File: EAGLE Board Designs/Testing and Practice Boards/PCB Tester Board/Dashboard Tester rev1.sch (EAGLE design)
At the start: 32 parts, among them J1 CONNECTOR-CAN_NF_T_V_BLACK, J2 CONNECTOR-6_NF_T_V_BLACK, J3 CONNECTOR-8_NF_T_V_BLACK, Q1 TRANSISTOR_N_MOS_PMV15ENEA, Q10 TRANSISTOR_N_MOS_PMV15ENEA, Q11 TRANSISTOR_P_MOS_SOT23_SI2369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, Q2 TRANSISTOR_N_MOS_PMV15ENEA, Q3 TRANSISTOR_N_MOS_PMV15ENEA, Q4 TRANSISTOR_N_MOS_PMV15ENEA, Q5 TRANSISTOR_N_MOS_PMV15ENEA, Q6 TRANSISTOR_N_MOS_PMV15ENEA, Q7 TRANSISTOR_P_MOS_SOT23_SI2369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, Q8 TRANSISTOR_N_MOS_PMV15ENEA, Q9 TRANSISTOR_P_MOS_SOT23_SI2369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, U1 TEENSY_3.5, U2 CAN_TRANSCIEVER_TCAN1051HQV-Q1, U3 VOLTAGE_REGULATOR_OKI-78SR_5V

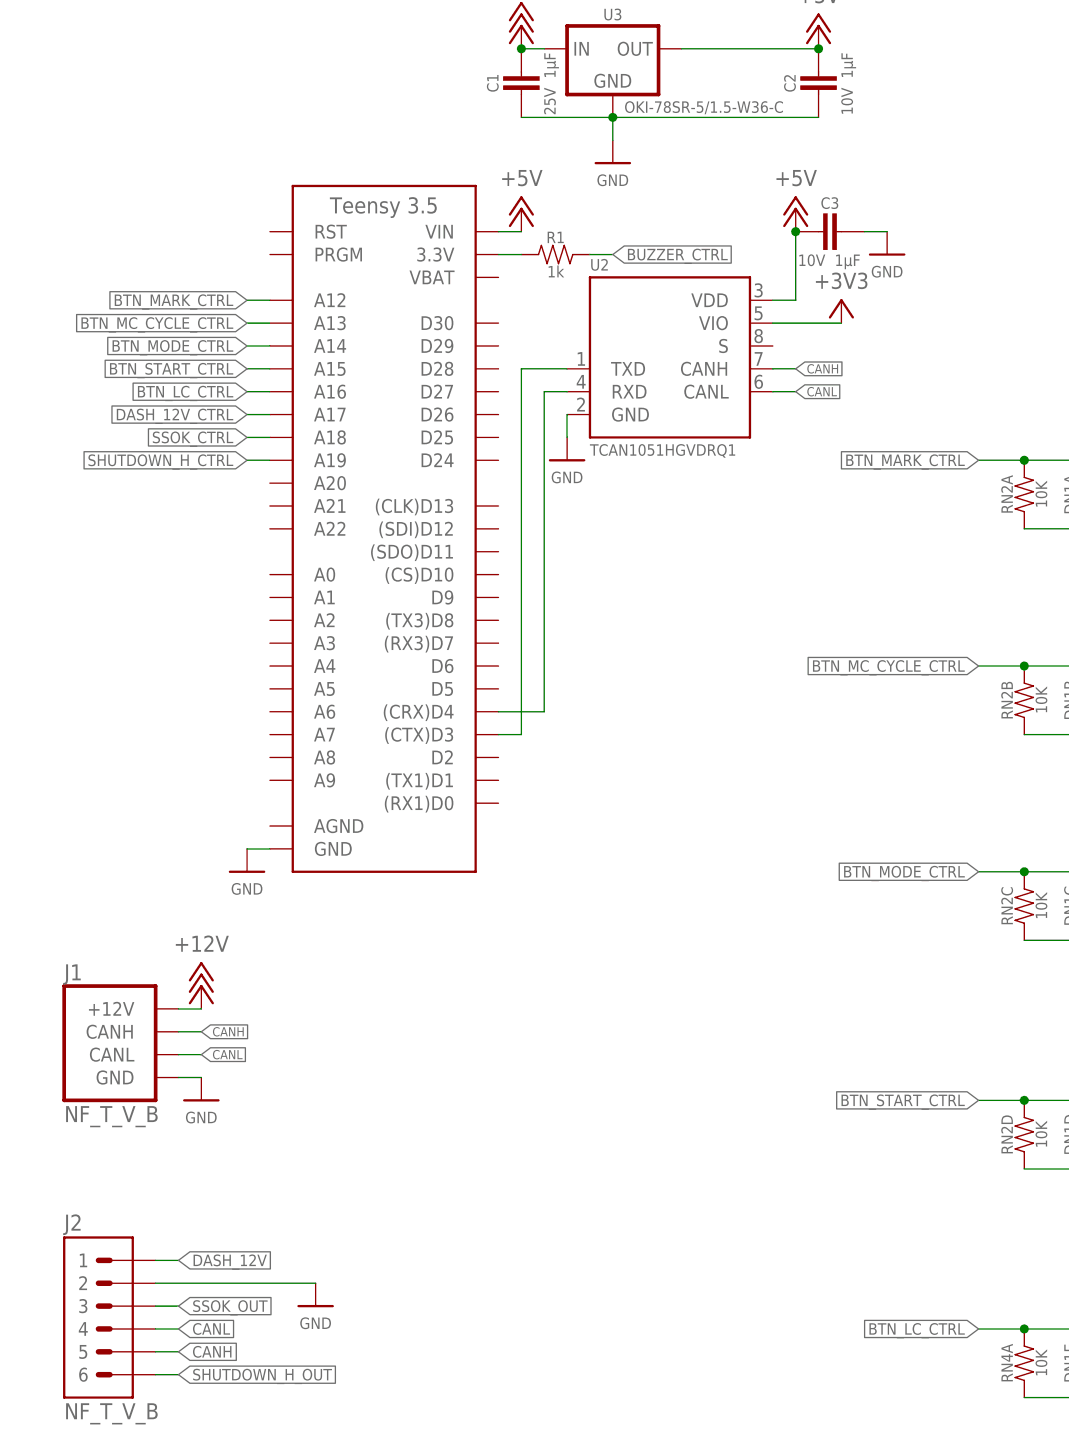
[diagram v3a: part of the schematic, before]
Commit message: Rearranged control-teensy connections
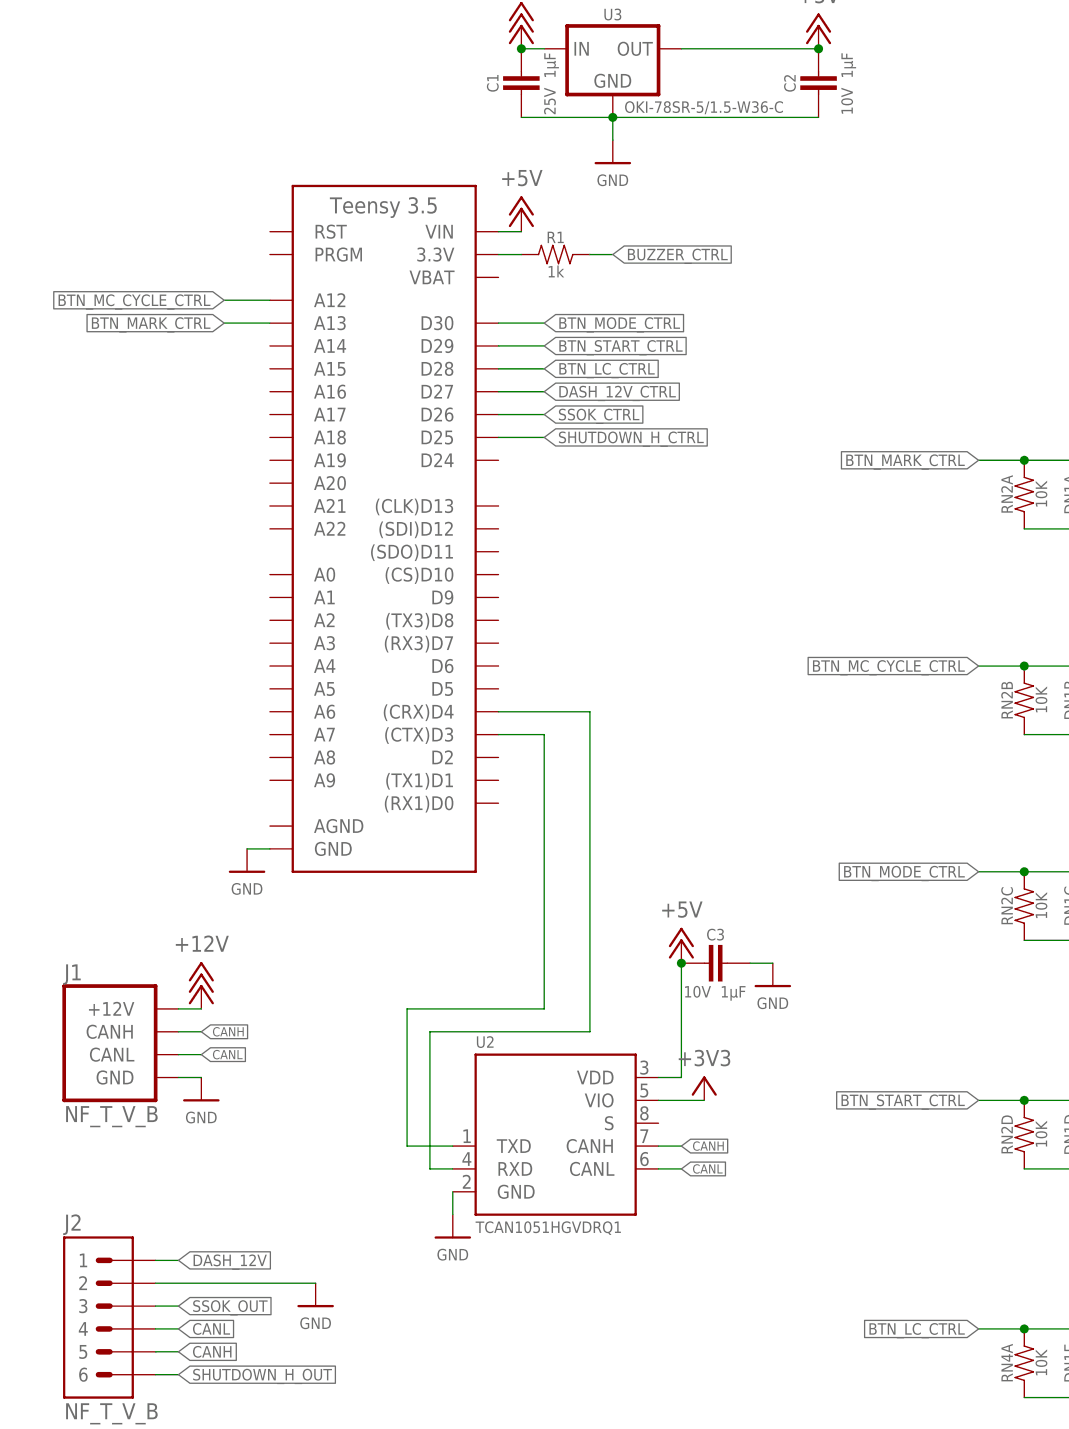
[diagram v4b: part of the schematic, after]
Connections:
- removed net N$5: U1.A17
- net BTN_LC_CTRL: now also U1.D28; no longer U1.A16
- net BTN_MARK_CTRL: now also U1.A13; no longer U1.A12
- net BTN_MC_CYCLE_CTRL: now also U1.A12; no longer U1.A13
- net BTN_MODE_CTRL: now also U1.D30; no longer U1.A14
- net BTN_START_CTRL: now also U1.D29; no longer U1.A15
- net DASH_12V_CTRL: now also U1.D27
- net SHUTDOWN_H_CTRL: now also U1.D25; no longer U1.A19
- net SSOK_CTRL: now also U1.D26; no longer U1.A18
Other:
- moved on the sheet: C3, U2

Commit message: Continuing trace work
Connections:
- removed net BUZZER_CTRL: J3.4
- net BTN_LAUNCH_CONTROL: now also J3.4; no longer J3.7
- net BTN_MARK: now also J3.8; no longer J3.2
- net BTN_MC_CYCLE: now also J3.7; no longer J3.3
- net BTN_MODE: now also J3.6; no longer J3.5
- net BTN_START: now also J3.5; no longer J3.6
- net DASH_12V: now also J3.1
- net SHUTDOWN_H_OUT: now also J3.3
- net SSOK_OUT: now also J3.2
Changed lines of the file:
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@@
 <label x="25.4" y="55.88" size="1.27" layer="95" xref="yes"/>
+</segment>
+<segment>
+<wire x1="22.86" y1="30.48" x2="27.94" y2="30.48" width="0.1524" layer="91"/>
+<label x="27.94" y="30.48" size="1.27" layer="95" xref="yes"/>
+<pinref part="J3" gate="G$1" pin="2"/>
 </segment>
 </net>
@@
 <label x="25.4" y="60.96" size="1.27" layer="95" xref="yes"/>
 </segment>
+<segment>
+<wire x1="22.86" y1="33.02" x2="27.94" y2="33.02" width="0.1524" layer="91"/>
+<label x="27.94" y="33.02" size="1.27" layer="95" xref="yes"/>
+<pinref part="J3" gate="G$1" pin="1"/>
+</segment>
 </net>
 <net name="SHUTDOWN_H_OUT" class="0">
@@
 <wire x1="22.86" y1="48.26" x2="25.4" y2="48.26" width="0.1524" layer="91"/>
 <label x="25.4" y="48.26" size="1.27" layer="95" xref="yes"/>
+</segment>
+<segment>
+<wire x1="22.86" y1="27.94" x2="27.94" y2="27.94" width="0.1524" layer="91"/>
+<label x="27.94" y="27.94" size="1.27" layer="95" xref="yes"/>
+<pinref part="J3" gate="G$1" pin="3"/>
 </segment>
 </net>
@@
 <net name="BTN_MARK" class="0">
 <segment>
-<pinref part="J3" gate="G$1" pin="2"/>
-<wire x1="22.86" y1="30.48" x2="25.4" y2="30.48" width="0.1524" layer="91"/>
-<label x="25.4" y="30.48" size="1.27" layer="95" xref="yes"/>
-</segment>
-<segment>
 <pinref part="Q1" gate="G$1" pin="D"/>
 <wire x1="149.86" y1="154.94" x2="154.94" y2="154.94" width="0.1524" layer="91"/>
 <label x="154.94" y="154.94" size="1.27" layer="95" xref="yes"/>
 </segment>
+<segment>
+<wire x1="22.86" y1="15.24" x2="27.94" y2="15.24" width="0.1524" layer="91"/>
+<label x="27.94" y="15.24" size="1.27" layer="95" xref="yes"/>
+<pinref part="J3" gate="G$1" pin="8"/>
+</segment>
 </net>
 <net name="BTN_MC_CYCLE" class="0">
-<segment>
-<pinref part="J3" gate="G$1" pin="3"/>
-<wire x1="22.86" y1="27.94" x2="25.4" y2="27.94" width="0.1524" layer="91"/>
-<label x="25.4" y="27.94" size="1.27" layer="95" xref="yes"/>
-</segment>
 <segment>
 <pinref part="Q2" gate="G$1" pin="D"/>
@@
 <label x="154.94" y="132.08" size="1.27" layer="95" xref="yes"/>
 </segment>
-</net>
-<net name="BUZZER_CTRL" class="0">
 <segment>
-<pinref part="J3" gate="G$1" pin="4"/>
-<wire x1="22.86" y1="25.4" x2="25.4" y2="25.4" width="0.1524" layer="91"/>
-<label x="25.4" y="25.4" size="1.27" layer="95" xref="yes"/>
-<label x="73.66" y="172.72" size="1.27" layer="95" xref="yes"/>
+<wire x1="22.86" y1="17.78" x2="27.94" y2="17.78" width="0.1524" layer="91"/>
+<label x="27.94" y="17.78" size="1.27" layer="95" xref="yes"/>
+<pinref part="J3" gate="G$1" pin="7"/>
 </segment>
 </net>
 <net name="BTN_MODE" class="0">
-<segment>
-<pinref part="J3" gate="G$1" pin="5"/>
-<wire x1="22.86" y1="22.86" x2="25.4" y2="22.86" width="0.1524" layer="91"/>
-<label x="25.4" y="22.86" size="1.27" layer="95" xref="yes"/>
-</segment>
 <segment>
 <pinref part="Q3" gate="G$1" pin="D"/>
@@
 <label x="154.94" y="109.22" size="1.27" layer="95" xref="yes"/>
 </segment>
+<segment>
+<wire x1="22.86" y1="20.32" x2="27.94" y2="20.32" width="0.1524" layer="91"/>
+<label x="27.94" y="20.32" size="1.27" layer="95" xref="yes"/>
+<pinref part="J3" gate="G$1" pin="6"/>
+</segment>
 </net>
 <net name="BTN_START" class="0">
-<segment>
-<pinref part="J3" gate="G$1" pin="6"/>
-<wire x1="22.86" y1="20.32" x2="25.4" y2="20.32" width="0.1524" layer="91"/>
-<label x="25.4" y="20.32" size="1.27" layer="95" xref="yes"/>
-</segment>
 <segment>
 <pinref part="Q4" gate="G$1" pin="D"/>
@@
 <label x="154.94" y="83.82" size="1.27" layer="95" xref="yes"/>
 </segment>
+<segment>
+<wire x1="22.86" y1="22.86" x2="27.94" y2="22.86" width="0.1524" layer="91"/>
+<label x="27.94" y="22.86" size="1.27" layer="95" xref="yes"/>
+<pinref part="J3" gate="G$1" pin="5"/>
+</segment>
 </net>
 <net name="BTN_LAUNCH_CONTROL" class="0">
-<segment>
-<pinref part="J3" gate="G$1" pin="7"/>
-<wire x1="22.86" y1="17.78" x2="25.4" y2="17.78" width="0.1524" layer="91"/>
-<label x="25.4" y="17.78" size="1.27" layer="95" xref="yes"/>
-</segment>
 <segment>
 <pinref part="Q5" gate="G$1" pin="D"/>
@@
 <label x="154.94" y="58.42" size="1.27" layer="95" xref="yes"/>
 </segment>
+<segment>
+<wire x1="22.86" y1="25.4" x2="27.94" y2="25.4" width="0.1524" layer="91"/>
+<label x="27.94" y="25.4" size="1.27" layer="95" xref="yes"/>
+<pinref part="J3" gate="G$1" pin="4"/>
+</segment>
 </net>

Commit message: Finished tracing
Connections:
- net BTN_LAUNCH_CONTROL: now also J3.1; no longer J3.4
- net DASH_12V: now also J3.4; no longer J3.1
- net SHUTDOWN_H_OUT: no longer J3.3
- net SSOK_OUT: no longer J3.2
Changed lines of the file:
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@@
 <label x="25.4" y="55.88" size="1.27" layer="95" xref="yes"/>
-</segment>
-<segment>
-<wire x1="22.86" y1="30.48" x2="27.94" y2="30.48" width="0.1524" layer="91"/>
-<label x="27.94" y="30.48" size="1.27" layer="95" xref="yes"/>
-<pinref part="J3" gate="G$1" pin="2"/>
 </segment>
 </net>
@@
 </segment>
 <segment>
-<wire x1="22.86" y1="33.02" x2="27.94" y2="33.02" width="0.1524" layer="91"/>
-<label x="27.94" y="33.02" size="1.27" layer="95" xref="yes"/>
-<pinref part="J3" gate="G$1" pin="1"/>
+<wire x1="22.86" y1="25.4" x2="27.94" y2="25.4" width="0.1524" layer="91"/>
+<label x="27.94" y="25.4" size="1.27" layer="95" xref="yes"/>
+<pinref part="J3" gate="G$1" pin="4"/>
 </segment>
 </net>
@@
 <wire x1="22.86" y1="48.26" x2="25.4" y2="48.26" width="0.1524" layer="91"/>
 <label x="25.4" y="48.26" size="1.27" layer="95" xref="yes"/>
-</segment>
-<segment>
-<wire x1="22.86" y1="27.94" x2="27.94" y2="27.94" width="0.1524" layer="91"/>
-<label x="27.94" y="27.94" size="1.27" layer="95" xref="yes"/>
-<pinref part="J3" gate="G$1" pin="3"/>
 </segment>
 </net>
@@
 </segment>
 <segment>
-<wire x1="22.86" y1="25.4" x2="27.94" y2="25.4" width="0.1524" layer="91"/>
-<label x="27.94" y="25.4" size="1.27" layer="95" xref="yes"/>
-<pinref part="J3" gate="G$1" pin="4"/>
+<wire x1="22.86" y1="33.02" x2="27.94" y2="33.02" width="0.1524" layer="91"/>
+<label x="27.94" y="33.02" size="1.27" layer="95" xref="yes"/>
+<pinref part="J3" gate="G$1" pin="1"/>
 </segment>
 </net>

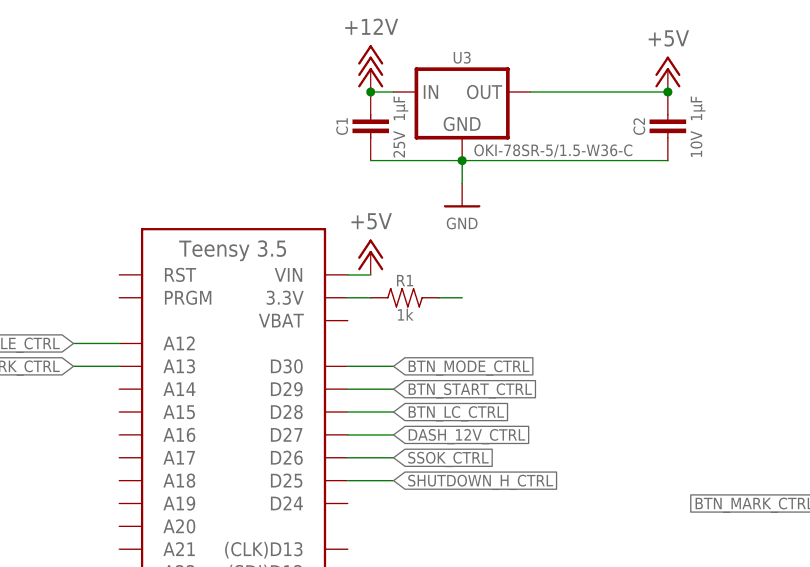
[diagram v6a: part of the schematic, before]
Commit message: Fixed 3v3 connection
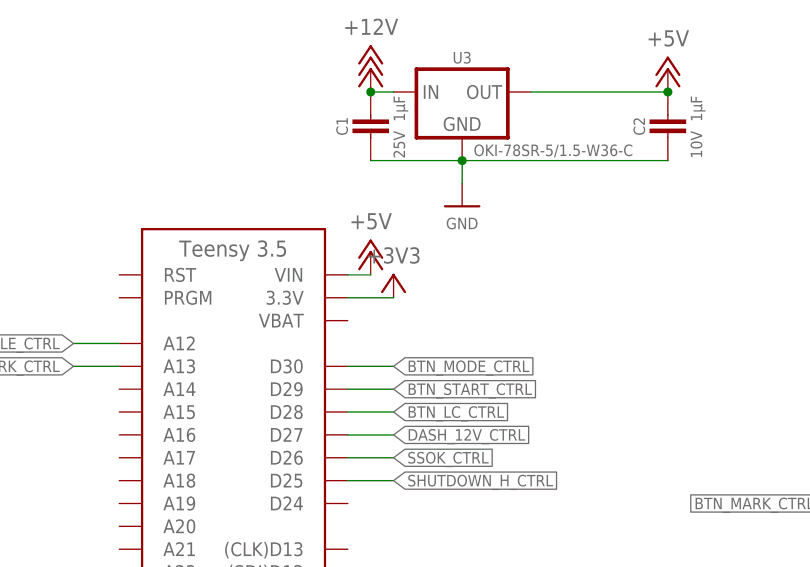
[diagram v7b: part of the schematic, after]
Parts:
- removed R1: 1k, HyTechDevices:RESISTOR0603
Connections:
- removed net N$7: R1.1, U1.3.3V
- removed net N$9: R1.2
- net +3V3: now also U1.3.3V
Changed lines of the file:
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@@
 <part name="C3" library="HyTechDevices" deviceset="CAPACITOR_?_*" device="0603" technology="10V_1UF"/>
 <part name="GND14" library="HyTechSupplies" deviceset="GND" device=""/>
-<part name="R1" library="HyTechDevices" deviceset="RESISTOR" device="0603" value="1k"/>
+<part name="+3V2" library="HyTechSupplies" deviceset="+3V3" device=""/>
 </parts>
 <sheets>
@@
 <attribute name="VALUE" x="91.44" y="90.17" size="1.27" layer="96" align="top-center"/>
 </instance>
-<instance part="R1" gate="G$1" x="68.58" y="172.72" smashed="yes">
-<attribute name="NAME" x="67.31" y="173.99" size="1.27" layer="95" align="bottom-center"/>
-<attribute name="VALUE" x="67.31" y="171.45" size="1.27" layer="96" align="top-center"/>
+<instance part="+3V2" gate="G$1" x="66.04" y="175.26" smashed="yes">
+<attribute name="VALUE" x="66.04" y="176.53" size="1.778" layer="96" align="bottom-center"/>
 </instance>
 </instances>
@@
 <wire x1="78.74" y1="78.74" x2="83.82" y2="78.74" width="0.1524" layer="91"/>
 </segment>
+<segment>
+<pinref part="+3V2" gate="G$1" pin="+3V3"/>
+<wire x1="60.96" y1="172.72" x2="66.04" y2="172.72" width="0.1524" layer="91"/>
+<pinref part="U1" gate="G$1" pin="3.3V"/>
+</segment>
 </net>
 <net name="CANH" class="0">
@@
 </segment>
 </net>
-<net name="N$7" class="0">
-<segment>
-<pinref part="U1" gate="G$1" pin="3.3V"/>
-<pinref part="R1" gate="G$1" pin="1"/>
-<wire x1="60.96" y1="172.72" x2="63.5" y2="172.72" width="0.1524" layer="91"/>
-</segment>
-</net>
-<net name="N$9" class="0">
-<segment>
-<pinref part="R1" gate="G$1" pin="2"/>
-<wire x1="71.12" y1="172.72" x2="73.66" y2="172.72" width="0.1524" layer="91"/>
-</segment>
-</net>

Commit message: Flipped circuit
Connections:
- net BTN_LAUNCH_CONTROL: no longer J3.1
- net BTN_MARK: now also J3.2; no longer J3.8
- net BTN_MC_CYCLE: now also J3.3; no longer J3.7
- net BTN_MODE: no longer J3.6
- net BTN_START: no longer J3.5
- net DASH_12V: no longer J3.4
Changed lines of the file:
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@@
 <label x="25.4" y="60.96" size="1.27" layer="95" xref="yes"/>
-</segment>
-<segment>
-<wire x1="22.86" y1="25.4" x2="27.94" y2="25.4" width="0.1524" layer="91"/>
-<label x="27.94" y="25.4" size="1.27" layer="95" xref="yes"/>
-<pinref part="J3" gate="G$1" pin="4"/>
 </segment>
 </net>
@@
 </segment>
 <segment>
-<wire x1="22.86" y1="15.24" x2="27.94" y2="15.24" width="0.1524" layer="91"/>
-<label x="27.94" y="15.24" size="1.27" layer="95" xref="yes"/>
-<pinref part="J3" gate="G$1" pin="8"/>
+<wire x1="22.86" y1="30.48" x2="27.94" y2="30.48" width="0.1524" layer="91"/>
+<label x="27.94" y="30.48" size="1.27" layer="95" xref="yes"/>
+<pinref part="J3" gate="G$1" pin="2"/>
 </segment>
 </net>
@@
 </segment>
 <segment>
-<wire x1="22.86" y1="17.78" x2="27.94" y2="17.78" width="0.1524" layer="91"/>
-<label x="27.94" y="17.78" size="1.27" layer="95" xref="yes"/>
-<pinref part="J3" gate="G$1" pin="7"/>
+<wire x1="22.86" y1="27.94" x2="27.94" y2="27.94" width="0.1524" layer="91"/>
+<label x="27.94" y="27.94" size="1.27" layer="95" xref="yes"/>
+<pinref part="J3" gate="G$1" pin="3"/>
 </segment>
 </net>
@@
 <label x="154.94" y="109.22" size="1.27" layer="95" xref="yes"/>
 </segment>
-<segment>
-<wire x1="22.86" y1="20.32" x2="27.94" y2="20.32" width="0.1524" layer="91"/>
-<label x="27.94" y="20.32" size="1.27" layer="95" xref="yes"/>
-<pinref part="J3" gate="G$1" pin="6"/>
-</segment>
 </net>
 <net name="BTN_START" class="0">
@@
 <wire x1="149.86" y1="83.82" x2="154.94" y2="83.82" width="0.1524" layer="91"/>
 <label x="154.94" y="83.82" size="1.27" layer="95" xref="yes"/>
-</segment>
-<segment>
-<wire x1="22.86" y1="22.86" x2="27.94" y2="22.86" width="0.1524" layer="91"/>
-<label x="27.94" y="22.86" size="1.27" layer="95" xref="yes"/>
-<pinref part="J3" gate="G$1" pin="5"/>
 </segment>
 </net>
@@
 <label x="154.94" y="58.42" size="1.27" layer="95" xref="yes"/>
 </segment>
-<segment>
-<wire x1="22.86" y1="33.02" x2="27.94" y2="33.02" width="0.1524" layer="91"/>
-<label x="27.94" y="33.02" size="1.27" layer="95" xref="yes"/>
-<pinref part="J3" gate="G$1" pin="1"/>
-</segment>
 </net>
